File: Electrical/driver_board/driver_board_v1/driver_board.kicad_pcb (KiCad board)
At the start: 2 copper layers, 7 parts, among them U1 ESP32-WROOM-32

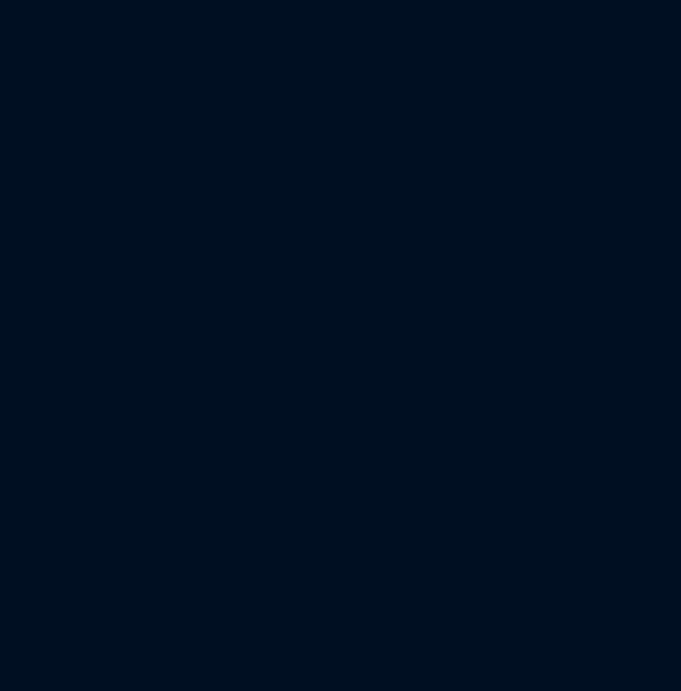
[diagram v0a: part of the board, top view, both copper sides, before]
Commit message: Updated driver board v1
New dip switch allignment and assigned first footprints
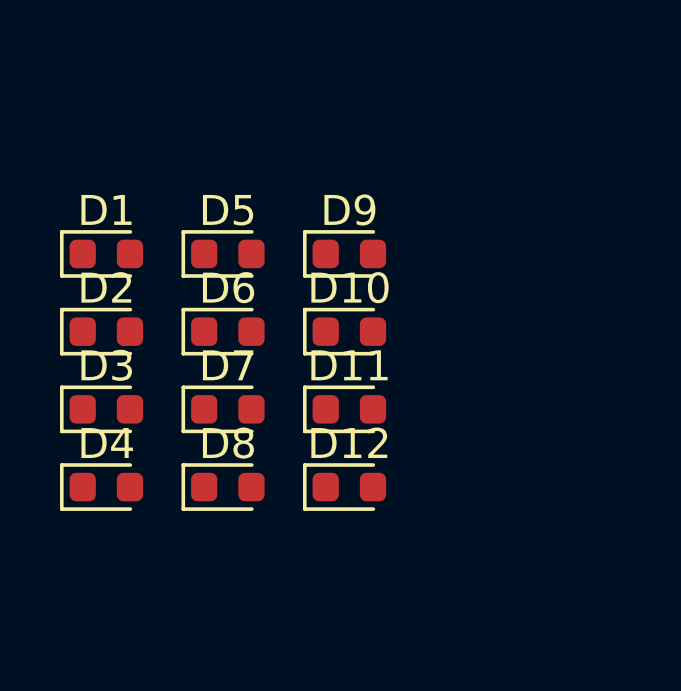
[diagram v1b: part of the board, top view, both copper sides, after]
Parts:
- added D1: LED, LED_SMD:LED_0603_1608Metric, F.Cu at (31.8, 83.7)
- added D10: LED, LED_SMD:LED_0603_1608Metric, F.Cu at (39.9, 86.3)
- added D11: LED, LED_SMD:LED_0603_1608Metric, F.Cu at (39.9, 88.8)
- added D12: LED, LED_SMD:LED_0603_1608Metric, F.Cu at (39.9, 91.4)
- added D2: LED, LED_SMD:LED_0603_1608Metric, F.Cu at (31.8, 86.3)
- added D3: LED, LED_SMD:LED_0603_1608Metric, F.Cu at (31.8, 88.8)
- added D4: LED, LED_SMD:LED_0603_1608Metric, F.Cu at (31.8, 91.4)
- added D5: LED, LED_SMD:LED_0603_1608Metric, F.Cu at (35.8, 83.7)
- added D6: LED, LED_SMD:LED_0603_1608Metric, F.Cu at (35.8, 86.3)
- added D7: LED, LED_SMD:LED_0603_1608Metric, F.Cu at (35.8, 88.8)
- added D8: LED, LED_SMD:LED_0603_1608Metric, F.Cu at (35.8, 91.4)
- added D9: LED, LED_SMD:LED_0603_1608Metric, F.Cu at (39.9, 83.7)
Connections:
- A1 pad 10: Net-(A1-MS1) -> IO33
- A1 pad 11: Net-(A1-MS2) -> IO34
- A1 pad 12: Net-(A1-MS3) -> IO35
- A1 pad 13: Net-(A1-~{RESET}) -> IO14
- A2 pad 10: Net-(A2-MS1) -> IO33
- A2 pad 11: Net-(A2-MS2) -> IO34
- A2 pad 12: Net-(A2-MS3) -> IO35
- A2 pad 13: Net-(A2-~{RESET}) -> IO13
- A3 pad 10: Net-(A3-MS1) -> IO33
- A3 pad 11: Net-(A3-MS2) -> IO34
- A3 pad 12: Net-(A3-MS3) -> IO35
- A3 pad 13: Net-(A3-~{RESET}) -> IO12
- A4 pad 10: Net-(A4-MS1) -> IO33
- A4 pad 11: Net-(A4-MS2) -> IO34
- A4 pad 12: Net-(A4-MS3) -> IO35
- A4 pad 13: Net-(A4-~{RESET}) -> IO5
- A5 pad 10: Net-(A5-MS1) -> IO33
- A5 pad 11: Net-(A5-MS2) -> IO34
- A5 pad 12: Net-(A5-MS3) -> IO35
- A5 pad 13: Net-(A5-~{RESET}) -> IO4
- A6 pad 10: Net-(A6-MS1) -> IO33
- A6 pad 11: Net-(A6-MS2) -> IO34
- A6 pad 12: Net-(A6-MS3) -> IO35
- A6 pad 13: Net-(A6-~{RESET}) -> IO2
- U1 pad 13: unconnected-(U1-IO14-Pad13) -> IO14
- U1 pad 14: unconnected-(U1-IO12-Pad14) -> IO12
- U1 pad 16: unconnected-(U1-IO13-Pad16) -> IO13
- U1 pad 17: unconnected-(U1-SHD/SD2-Pad17) -> NC
- U1 pad 18: unconnected-(U1-SWP/SD3-Pad18) -> NC
- U1 pad 19: unconnected-(U1-SCS/CMD-Pad19) -> NC
- U1 pad 20: unconnected-(U1-SCK/CLK-Pad20) -> NC
- U1 pad 21: unconnected-(U1-SDO/SD0-Pad21) -> NC
- U1 pad 22: unconnected-(U1-SDI/SD1-Pad22) -> NC
- U1 pad 24: unconnected-(U1-IO2-Pad24) -> IO2
- U1 pad 25: unconnected-(U1-IO0-Pad25) -> NC
- U1 pad 26: unconnected-(U1-IO4-Pad26) -> IO4
- U1 pad 29: unconnected-(U1-IO5-Pad29) -> IO5
- U1 pad 3: unconnected-(U1-EN-Pad3) -> NC
- U1 pad 4: unconnected-(U1-SENSOR_VP-Pad4) -> NC
- U1 pad 5: unconnected-(U1-SENSOR_VN-Pad5) -> NC
- U1 pad 6: IO34 -> Net-(U1-IO34)
- U1 pad 7: IO35 -> Net-(U1-IO35)
- U1 pad 9: IO33 -> Net-(U1-IO33)
